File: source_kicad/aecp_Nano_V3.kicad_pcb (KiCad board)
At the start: 2 copper layers, 86.5 x 88 mm, 30 parts, among them P1 CONN_IGBT, P10 FIX, P11 FIX, P12 CONN_SEL2, P13 CONN_DEP2, P14 MP3V5050, P15 FIX, P16 FIX, P17 FIX, P18 FIX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

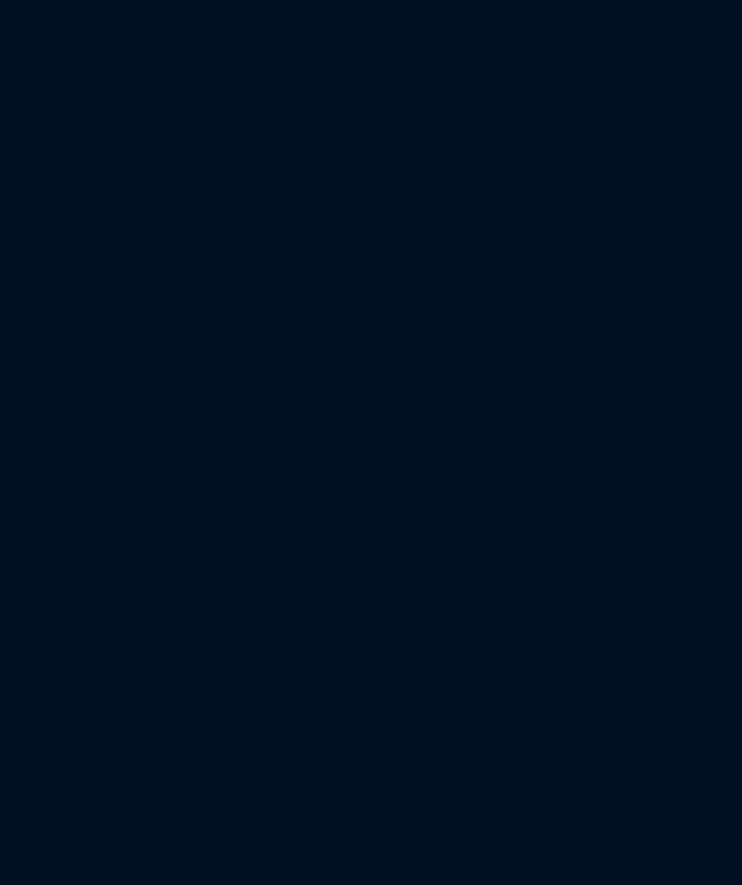
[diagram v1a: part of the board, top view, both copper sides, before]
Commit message: New source file for kicad with bluetooth adaptator
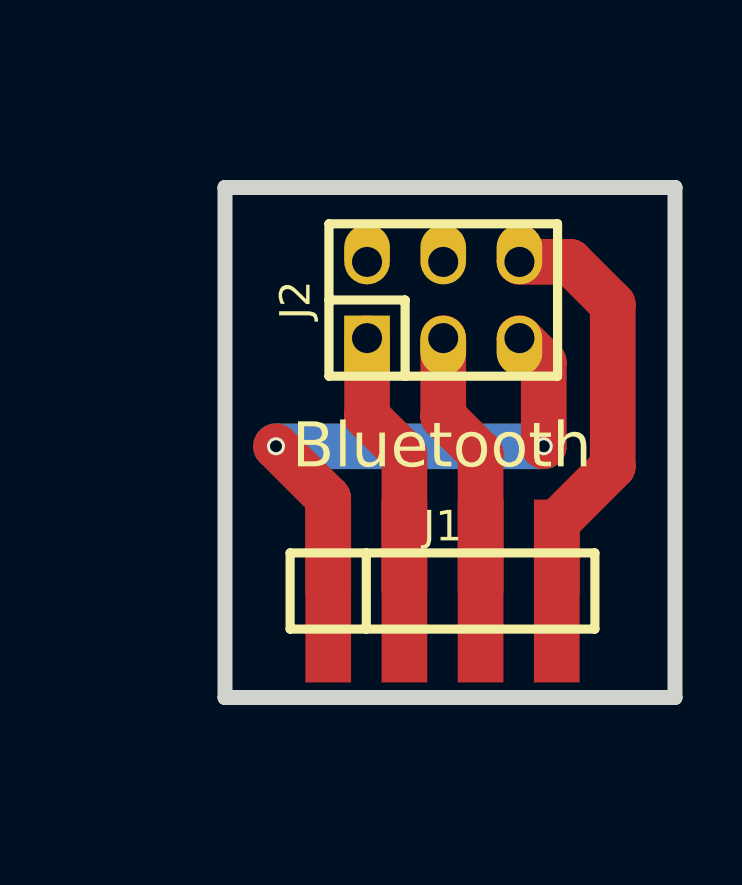
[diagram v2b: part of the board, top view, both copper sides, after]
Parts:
- added J1: CONN_HC06, w_pin_strip:pin_strip_4, F.Cu at (183.2, 63.5)
- added J2: CONN_ISP, w_pin_strip:pin_strip_3x2, F.Cu at (183.3, 53.8)
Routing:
- net Net-(J1-Pad1): track 0.00 -> 18.4 mm, vias 0 -> 2
- net Net-(J1-Pad4): track 0.00 -> 14.0 mm
- net Net-(J1-Pad3): track 0.00 -> 8.95 mm
- net Net-(J1-Pad2): track 0.00 -> 8.95 mm
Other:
- board size 86.5 x 88 mm -> 129.5 x 88 mm
- board text added: "Bluetooth"
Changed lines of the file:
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@@
-(kicad_pcb (version 4) (host pcbnew 4.0.4+e1-6308~48~ubuntu16.04.1-stable)
+(kicad_pcb (version 4) (host pcbnew 4.0.6-e0-6349~52~ubuntu16.10.1)
   (general
-    (links 34)
+    (links 38)
     (no_connects 2)
-    (area 61.249999 27.249999 148.249001 115.750001)
+    (area 61.249999 27.249999 202.849904 121.556881)
     (thickness 1.6)
-    (drawings 62)
-    (tracks 134)
+    (drawings 70)
+    (tracks 152)
     (zones 0)
-    (modules 30)
-    (nets 51)
+    (modules 32)
+    (nets 57)
   )
   (page A4)
@@
   )
   (setup
-    (last_trace_width 1.524)
+    (last_trace_width 0.25)
     (user_trace_width 0.508)
     (user_trace_width 0.762)
@@
     (mod_text_size 1 1)
     (mod_text_width 0.15)
-    (pad_size 1.5748 2.286)
-    (pad_drill 0)
+    (pad_size 1.524 1.99898)
+    (pad_drill 1)
     (pad_to_mask_clearance 0.2)
     (aux_axis_origin 0 0)
@@
   (net 49 "Net-(P18-Pad1)")
   (net 50 "Net-(U1-Pad7)")
+  (net 51 "Net-(J1-Pad1)")
+  (net 52 "Net-(J1-Pad2)")
+  (net 53 "Net-(J1-Pad3)")
+  (net 54 "Net-(J1-Pad4)")
+  (net 55 "Net-(J2-Pad2)")
+  (net 56 "Net-(J2-Pad4)")
   (net_class Default "Ceci est la Netclass par défaut"
     (clearance 0.2)
@@
     (add_net "Net-(C2-Pad2)")
     (add_net "Net-(C3-Pad2)")
+    (add_net "Net-(J1-Pad1)")
+    (add_net "Net-(J1-Pad2)")
+    (add_net "Net-(J1-Pad3)")
+    (add_net "Net-(J1-Pad4)")
+    (add_net "Net-(J2-Pad2)")
+    (add_net "Net-(J2-Pad4)")
     (add_net "Net-(P1-Pad1)")
     (add_net "Net-(P1-Pad2)")
@@
       (net 49 "Net-(P18-Pad1)"))
   )
+  (module w_pin_strip:pin_strip_4 (layer F.Cu)
+    (at 183.25 63.45)
+    (descr "Pin strip 4pin")
+    (tags "CONN DEV")
+    (fp_text reference J1 (at 0 -2.159) (layer F.SilkS)
+      (effects (font (size 1.016 1.016) (thickness 0.2032)))
+    )
+    (fp_text value CONN_HC06 (at 0.254 -3.556) (layer F.SilkS) hide
+      (effects (font (size 1.016 0.889) (thickness 0.2032)))
+    )
+    (fp_line (start -2.54 -1.27) (end -2.54 1.27) (layer F.SilkS) (width 0.3048))
+    (fp_line (start 5.08 1.27) (end -5.08 1.27) (layer F.SilkS) (width 0.3048))
+    (fp_line (start -5.08 -1.27) (end 5.08 -1.27) (layer F.SilkS) (width 0.3048))
+    (fp_line (start -5.08 1.27) (end -5.08 -1.27) (layer F.SilkS) (width 0.3048))
+    (fp_line (start 5.08 -1.27) (end 5.08 1.27) (layer F.SilkS) (width 0.3048))
+    (pad 1 smd rect (at -3.81 0) (size 1.524 6.096) (layers F.Cu F.Paste F.Mask)
+      (net 51 "Net-(J1-Pad1)"))
+    (pad 2 smd rect (at -1.27 0) (size 1.524 6.096) (layers F.Cu F.Paste F.Mask)
+      (net 52 "Net-(J1-Pad2)"))
+    (pad 3 smd rect (at 1.27 0) (size 1.524 6.096) (layers F.Cu F.Paste F.Mask)
+      (net 53 "Net-(J1-Pad3)"))
+    (pad 4 smd rect (at 3.81 0) (size 1.524 6.096) (layers F.Cu F.Paste F.Mask)
+      (net 54 "Net-(J1-Pad4)"))
+    (model walter/pin_strip/pin_strip_4.wrl
+      (at (xyz 0 0 0))
+      (scale (xyz 1 1 1))
+      (rotate (xyz 0 0 0))
+    )
+  )
+  (module w_pin_strip:pin_strip_3x2 (layer F.Cu)
+    (at 183.275 53.75)
+    (descr "Pin strip 3x2pin")
+    (tags "CONN DEV")
+    (fp_text reference J2 (at -4.925 0 90) (layer F.SilkS)
+      (effects (font (size 1.016 1.016) (thickness 0.2032)))
+    )
+    (fp_text value CONN_ISP (at 0 -5.08) (layer F.SilkS) hide
+      (effects (font (size 1.016 0.889) (thickness 0.2032)))
+    )
+    (fp_line (start -3.81 -2.54) (end 3.81 -2.54) (layer F.SilkS) (width 0.3048))
+    (fp_line (start 3.81 -2.54) (end 3.81 2.54) (layer F.SilkS) (width 0.3048))
+    (fp_line (start 3.81 2.54) (end -3.81 2.54) (layer F.SilkS) (width 0.3048))
+    (fp_line (start -3.81 0) (end -1.27 0) (layer F.SilkS) (width 0.3048))
+    (fp_line (start -1.27 0) (end -1.27 2.54) (layer F.SilkS) (width 0.3048))
+    (fp_line (start -3.81 -2.54) (end -3.81 2.54) (layer F.SilkS) (width 0.3048))
+    (pad 1 thru_hole rect (at -2.54 1.27) (size 1.524 1.99898) (drill 1 (offset 0 0.24892)) (layers *.Cu *.Mask F.SilkS)
+      (net 52 "Net-(J1-Pad2)"))
+    (pad 2 thru_hole oval (at -2.54 -1.27) (size 1.524 1.99898) (drill 1 (offset 0 -0.24892)) (layers *.Cu *.Mask F.SilkS)
+      (net 55 "Net-(J2-Pad2)"))
+    (pad 3 thru_hole oval (at 0 1.27) (size 1.524 1.99898) (drill 1 (offset 0 0.24892)) (layers *.Cu *.Mask F.SilkS)
+      (net 53 "Net-(J1-Pad3)"))
+    (pad 4 thru_hole oval (at 0 -1.27) (size 1.524 1.99898) (drill 1 (offset 0 -0.24892)) (layers *.Cu *.Mask F.SilkS)
+      (net 56 "Net-(J2-Pad4)"))
+    (pad 5 thru_hole oval (at 2.54 1.27) (size 1.524 1.99898) (drill 1 (offset 0 0.24892)) (layers *.Cu *.Mask F.SilkS)
+      (net 51 "Net-(J1-Pad1)"))
+    (pad 6 thru_hole oval (at 2.54 -1.27) (size 1.524 1.99898) (drill 1 (offset 0 -0.24892)) (layers *.Cu *.Mask F.SilkS)
+      (net 54 "Net-(J1-Pad4)"))
+    (model walter/pin_strip/pin_strip_3x2.wrl
+      (at (xyz 0 0 0))
+      (scale (xyz 1 1 1))
+      (rotate (xyz 0 0 0))
+    )
+  )
+  (dimension 15.425081 (width 0.3) (layer Cmts.User)
+    (gr_text "15,425 mm" (at 183.499491 72.549077 0.1857231081) (layer Cmts.User)
+      (effects (font (size 1.5 1.5) (thickness 0.3)))
+    )
+    (feature1 (pts (xy 191.2 68.825) (xy 191.216367 73.87407)))
+    (feature2 (pts (xy 175.775 68.875) (xy 175.791367 73.92407)))
+    (crossbar (pts (xy 175.782615 71.224084) (xy 191.207615 71.174084)))
+    (arrow1a (pts (xy 191.207615 71.174084) (xy 190.083018 71.764153)))
+    (arrow1b (pts (xy 191.207615 71.174084) (xy 190.079216 70.591318)))
+    (arrow2a (pts (xy 175.782615 71.224084) (xy 176.911014 71.80685)))
+    (arrow2b (pts (xy 175.782615 71.224084) (xy 176.907212 70.634015)))
+  )
+  (dimension 17.500071 (width 0.3) (layer Cmts.User)
+    (gr_text "17,500 mm" (at 196.349904 58.535071 89.83629822) (layer Cmts.User)
+      (effects (font (size 1.5 1.5) (thickness 0.3)))
+    )
+    (feature1 (pts (xy 192.8 67.275) (xy 197.674899 67.288928)))
+    (feature2 (pts (xy 192.85 49.775) (xy 197.724899 49.788928)))
+    (crossbar (pts (xy 195.02491 49.781214) (xy 194.97491 67.281214)))
+    (arrow1a (pts (xy 194.97491 67.281214) (xy 194.39171 66.153039)))
+    (arrow1b (pts (xy 194.97491 67.281214) (xy 195.564547 66.15639)))
+    (arrow2a (pts (xy 195.02491 49.781214) (xy 194.435273 50.906038)))
+    (arrow2b (pts (xy 195.02491 49.781214) (xy 195.60811 50.909389)))
+  )
+  (gr_text Bluetooth (at 183.25 58.5) (layer B.SilkS)
+    (effects (font (size 1.5 1.5) (thickness 0.3)) (justify mirror))
+  )
+  (gr_text Bluetooth (at 183.225 58.6) (layer F.SilkS)
+    (effects (font (size 1.5 1.5) (thickness 0.3)))
+  )
+  (gr_line (start 176 50) (end 176 67) (layer Edge.Cuts) (width 0.5))
+  (gr_line (start 191 50) (end 176 50) (layer Edge.Cuts) (width 0.5))
+  (gr_line (start 191 67) (end 191 50) (layer Edge.Cuts) (width 0.5))
+  (gr_line (start 176 67) (end 191 67) (layer Edge.Cuts) (width 0.5))
   (dimension 43.027967 (width 0.3) (layer Cmts.User)
     (gr_text "43,028 mm" (at 157.281212 51.262901 270.2367581) (layer Cmts.User)
@@
   (segment (start 75.57008 53.9623) (end 70.78218 58.7502) (width 2.032) (layer B.Cu) (net 19))
   (segment (start 77.29982 53.98516) (end 77.32268 53.9623) (width 1.016) (layer B.Cu) (net 19) (status 30))
-  (segment (start 77.32268 64.1223) (end 74.40168 64.1223) (width 1.524) (layer B.Cu) (net 20) (status 400000))
-  (segment (start 74.40168 64.1223) (end 69.46138 69.0626) (width 1.524) (layer B.Cu) (net 20) (status 800000))
+  (segment (start 77.32268 64.1223) (end 74.40168 64.1223) (width 1.524) (layer B.Cu) (net 20))
+  (segment (start 74.40168 64.1223) (end 69.46138 69.0626) (width 1.524) (layer B.Cu) (net 20))
   (segment (start 69.46138 69.0626) (end 69.53758 69.0626) (width 1.524) (layer B.Cu) (net 20))
   (segment (start 69.48678 38.227) (end 81.62798 38.227) (width 2.032) (layer B.Cu) (net 21))
@@
   (segment (start 78.82128 94.7674) (end 82.40268 98.3488) (width 2.032) (layer B.Cu) (net 45))
   (segment (start 82.37728 98.3234) (end 82.40268 98.3488) (width 1.524) (layer B.Cu) (net 45) (status 30))
+  (segment (start 186.625 58.625) (end 186.625 55.83) (width 1.524) (layer F.Cu) (net 51))
+  (segment (start 186.625 55.83) (end 185.815 55.02) (width 1.524) (layer F.Cu) (net 51))
+  (segment (start 177.7 58.625) (end 186.625 58.625) (width 1.524) (layer B.Cu) (net 51))
+  (via (at 186.625 58.625) (size 0.6) (drill 0.4) (layers F.Cu B.Cu) (net 51))
+  (segment (start 179.44 63.45) (end 179.44 60.365) (width 1.524) (layer F.Cu) (net 51))
+  (segment (start 179.44 60.365) (end 177.7 58.625) (width 1.524) (layer F.Cu) (net 51))
+  (via (at 177.7 58.625) (size 0.6) (drill 0.4) (layers F.Cu B.Cu) (net 51))
+  (segment (start 181.98 63.45) (end 181.98 58.878) (width 1.524) (layer F.Cu) (net 52))
+  (segment (start 181.98 58.878) (end 180.735 57.633) (width 1.524) (layer F.Cu) (net 52))
+  (segment (start 180.735 57.633) (end 180.735 55.02) (width 1.524) (layer F.Cu) (net 52))
+  (segment (start 184.52 63.45) (end 184.52 58.878) (width 1.524) (layer F.Cu) (net 53))
+  (segment (start 184.52 58.878) (end 183.275 57.633) (width 1.524) (layer F.Cu) (net 53))
+  (segment (start 183.275 57.633) (end 183.275 55.02) (width 1.524) (layer F.Cu) (net 53))
+  (segment (start 188.925 53.9) (end 187.505 52.48) (width 1.524) (layer F.Cu) (net 54))
+  (segment (start 187.505 52.48) (end 185.815 52.48) (width 1.524) (layer F.Cu) (net 54))
+  (segment (start 188.925 59.299) (end 188.925 53.9) (width 1.524) (layer F.Cu) (net 54))
+  (segment (start 187.06 63.45) (end 187.06 61.164) (width 1.524) (layer F.Cu) (net 54))
+  (segment (start 187.06 61.164) (end 188.925 59.299) (width 1.524) (layer F.Cu) (net 54))
 )
